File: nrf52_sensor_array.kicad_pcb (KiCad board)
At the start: 2 copper layers, 55.5 x 33.1 mm, 58 parts, among them J1 CONN_01X08, J2 CONN_01X08, J3 CONN_01X08, J4 CONN_01X08, J5 CONN_01X08, J6 CONN_01X08, P1 CONN_2, P2 CONN_2, P3 CONN_2, U1 TPS2294x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

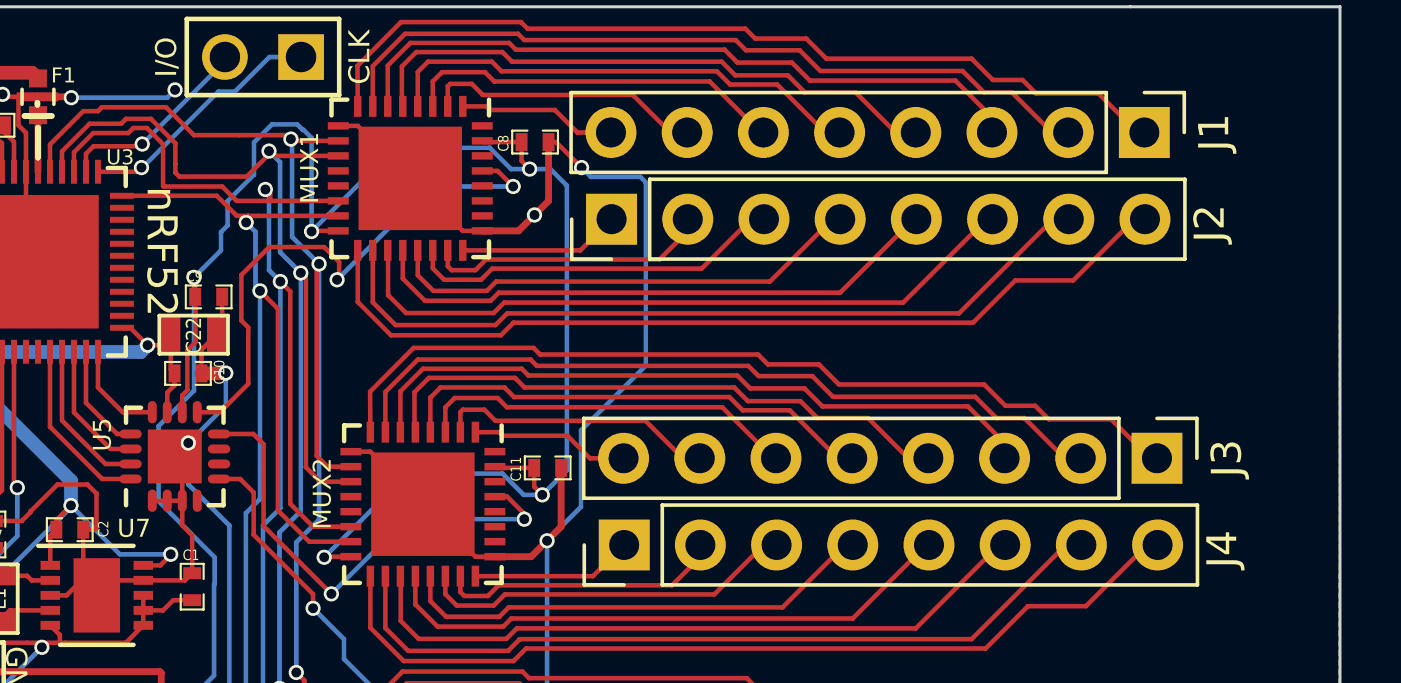
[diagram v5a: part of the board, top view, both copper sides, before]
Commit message: Updated .gitignore, added pins for 2 reference electrodes (grounded)
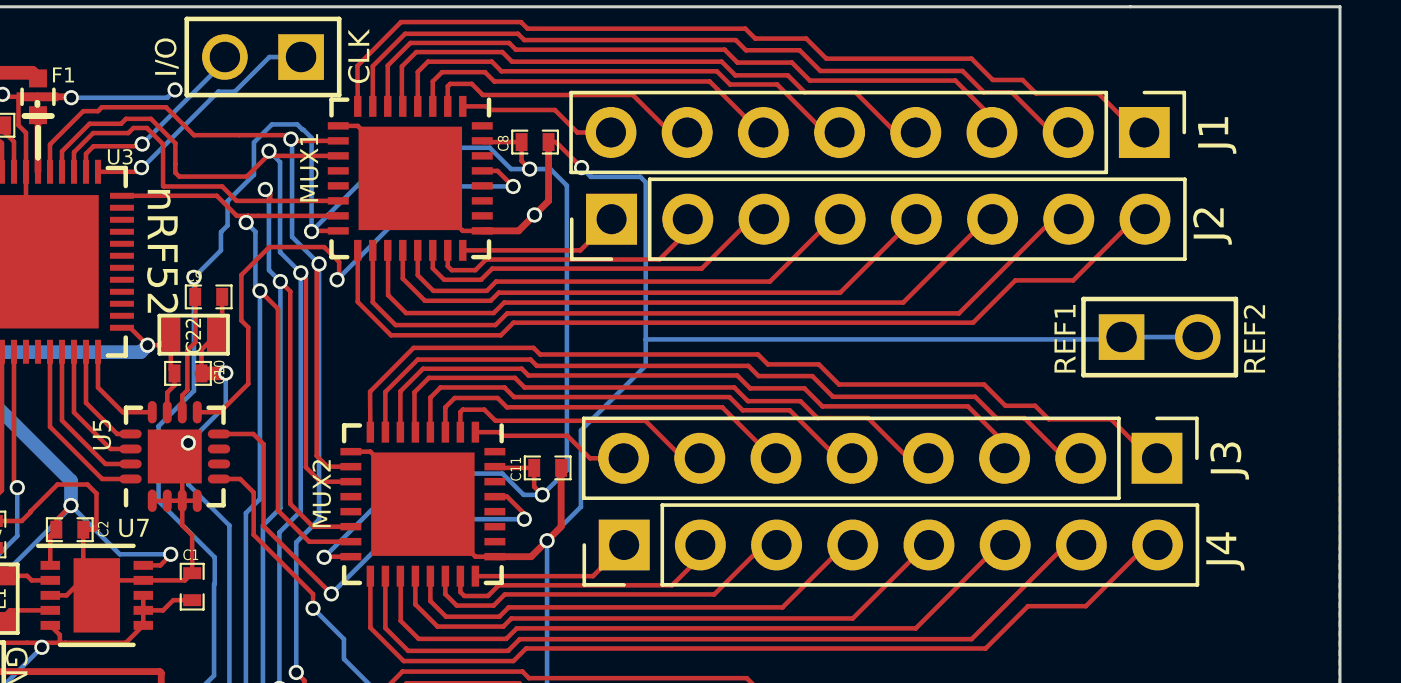
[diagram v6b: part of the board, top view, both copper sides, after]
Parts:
- added P4: CONN_2, PIN_ARRAY_2X1, F.Cu at (315.4, 136.5)
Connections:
- U5 pad 4: /meas_REFERENCE -> AVSS
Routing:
- net AVSS: track 217.4 -> 236.3 mm
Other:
- board text added: "REF1"
- board text added: "REF2"

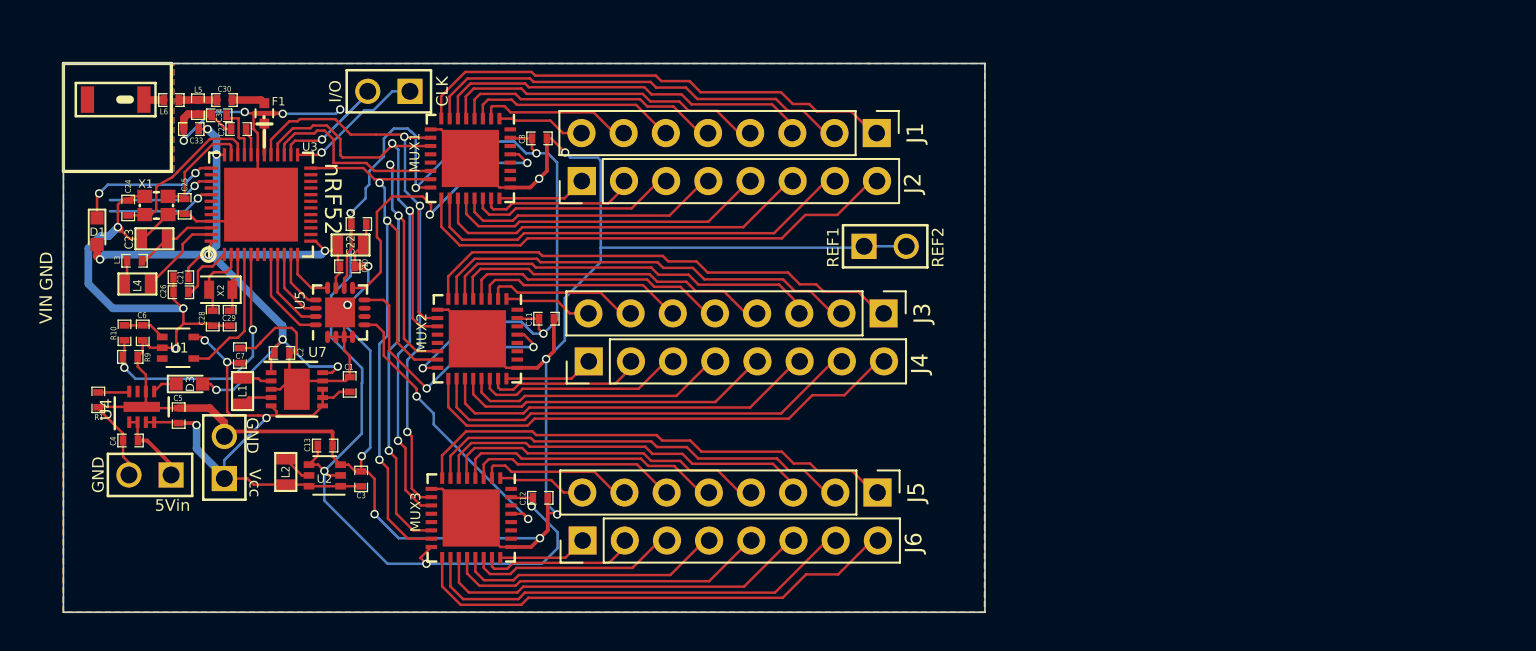
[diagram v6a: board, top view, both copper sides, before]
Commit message: Added option to short Reference electrodes to ground (using pad N1).
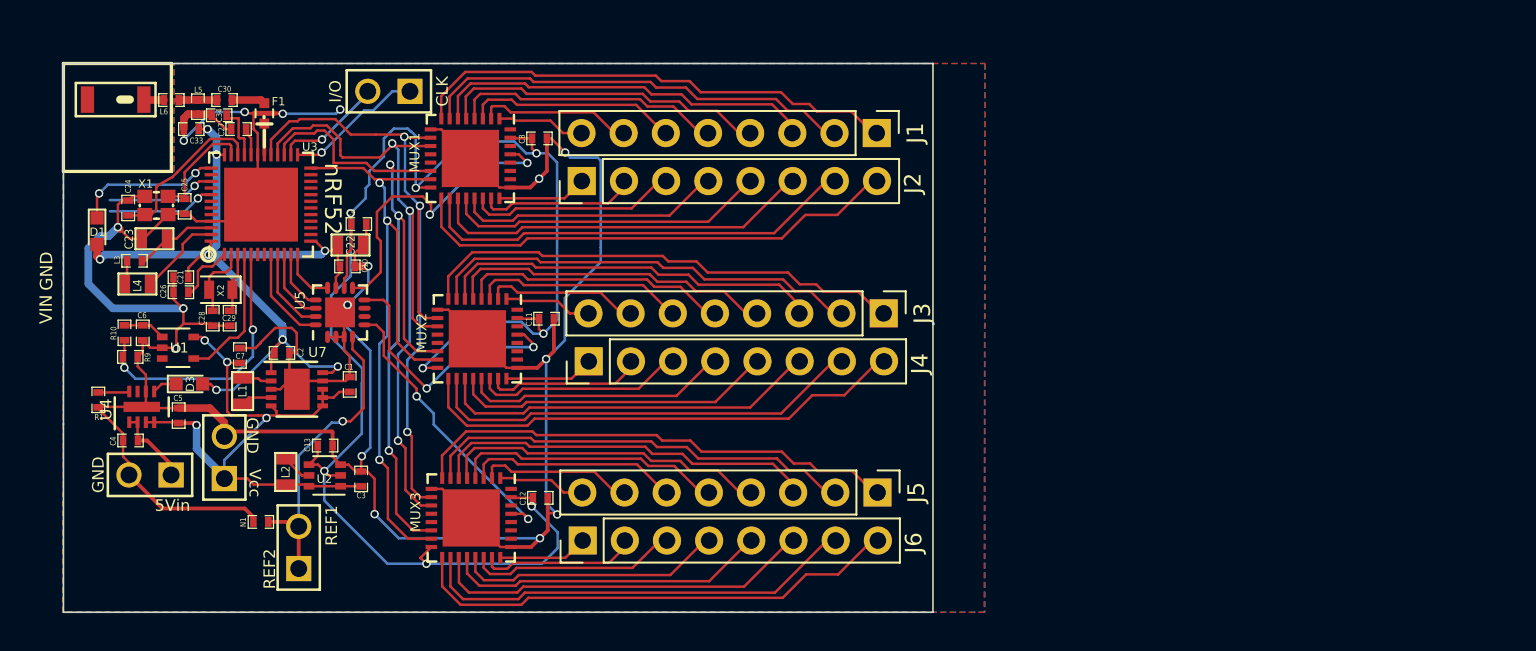
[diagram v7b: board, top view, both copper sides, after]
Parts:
- added N1: N.C., SM0402, F.Cu at (277.8, 153.1)
- moved P4 39.7 mm to (280.1, 154.7), turned to 90 degrees
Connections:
- P4 pad 1: AVSS -> /meas_REFERENCE
- P4 pad 2: AVSS -> /meas_REFERENCE
- U5 pad 4: AVSS -> /meas_REFERENCE
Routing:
- net /meas_REFERENCE: track 0.00 -> 18.4 mm, vias 0 -> 1
- net AVSS: track 236.3 -> 226.7 mm
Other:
- board size 55.5 x 33.1 mm -> 52.4 x 33.1 mm

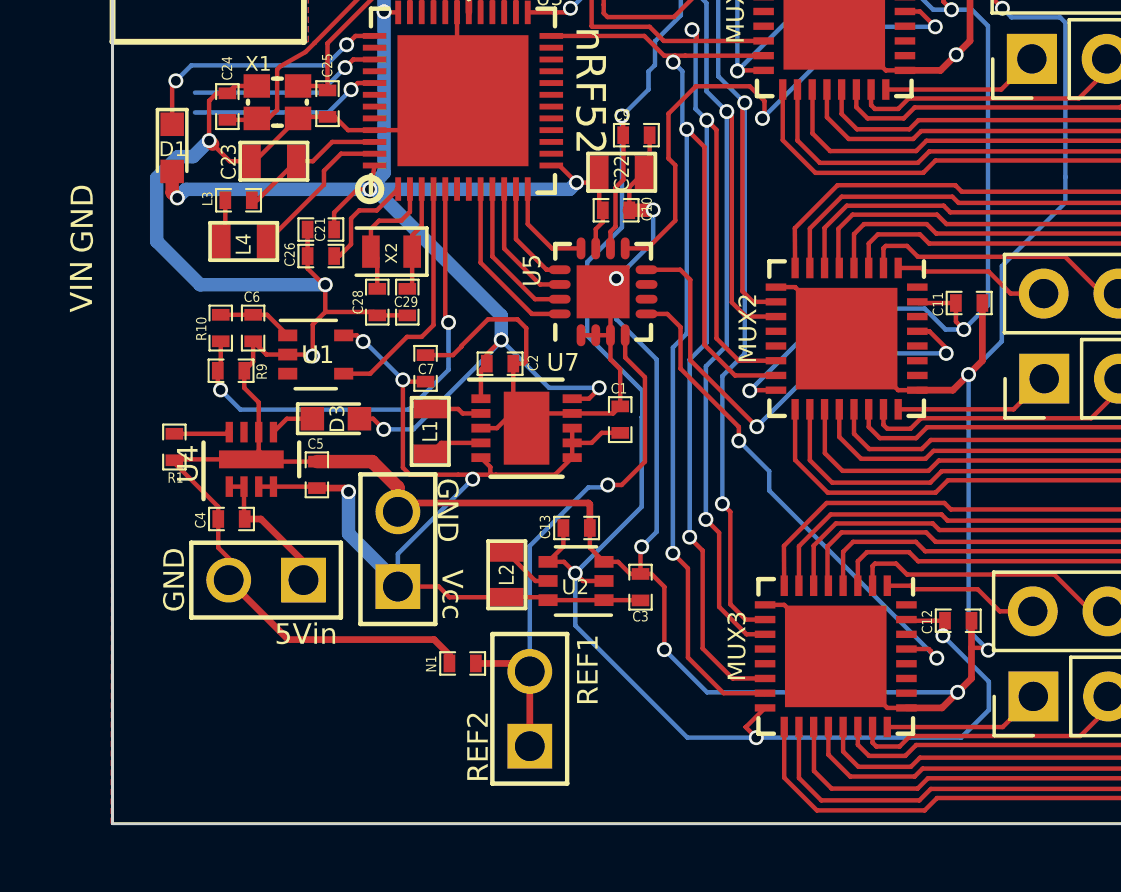
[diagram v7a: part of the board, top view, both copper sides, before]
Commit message: Added voltage divider, pins for 3v3 power supply.
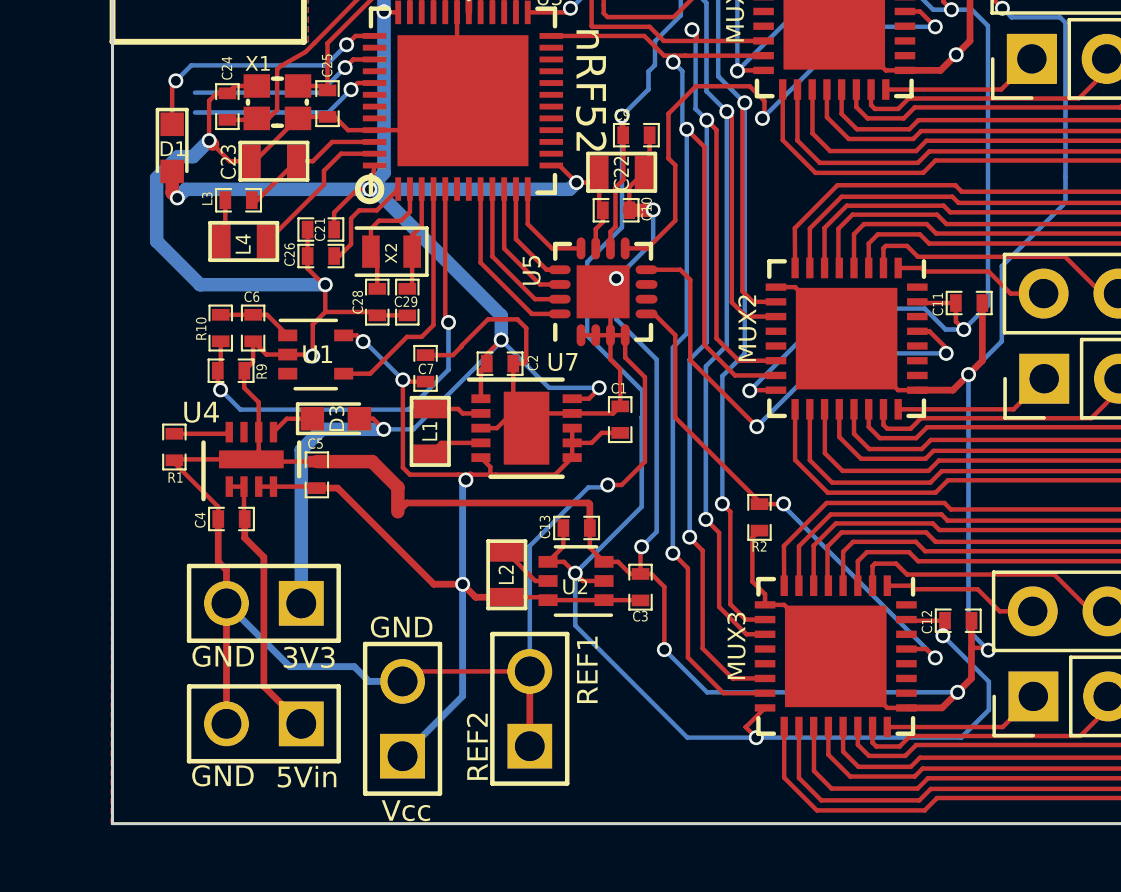
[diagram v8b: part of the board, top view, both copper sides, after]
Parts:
- removed N1: N.C., SM0402
- added P5: CONN_2, PIN_ARRAY_2X1, F.Cu at (271.0, 151.1)
- added R2: 2k, SM0402, F.Cu at (287.9, 148.2)
- moved P3 5.76 mm to (275.8, 155.0)
- moved P1 4.88 mm to (271.0, 155.2)
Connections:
- P4 pad 1: /meas_REFERENCE -> AVSS
- P4 pad 2: /meas_REFERENCE -> AVSS
- U5 pad 4: /meas_REFERENCE -> AVSS
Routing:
- net AVSS: track 226.7 -> 254.0 mm, vias 16 -> 17
- net /meas_REFERENCE: track 18.4 -> 0.00 mm, vias 1 -> 0
- net DVDD: track 52.2 -> 60.5 mm
- net VCC: track 36.6 -> 41.3 mm
- net 5V_in_charge: track 4.83 -> 9.36 mm
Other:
- board text added: "3V3"
- board text removed: "VIN"
